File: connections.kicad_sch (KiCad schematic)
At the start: 0 parts

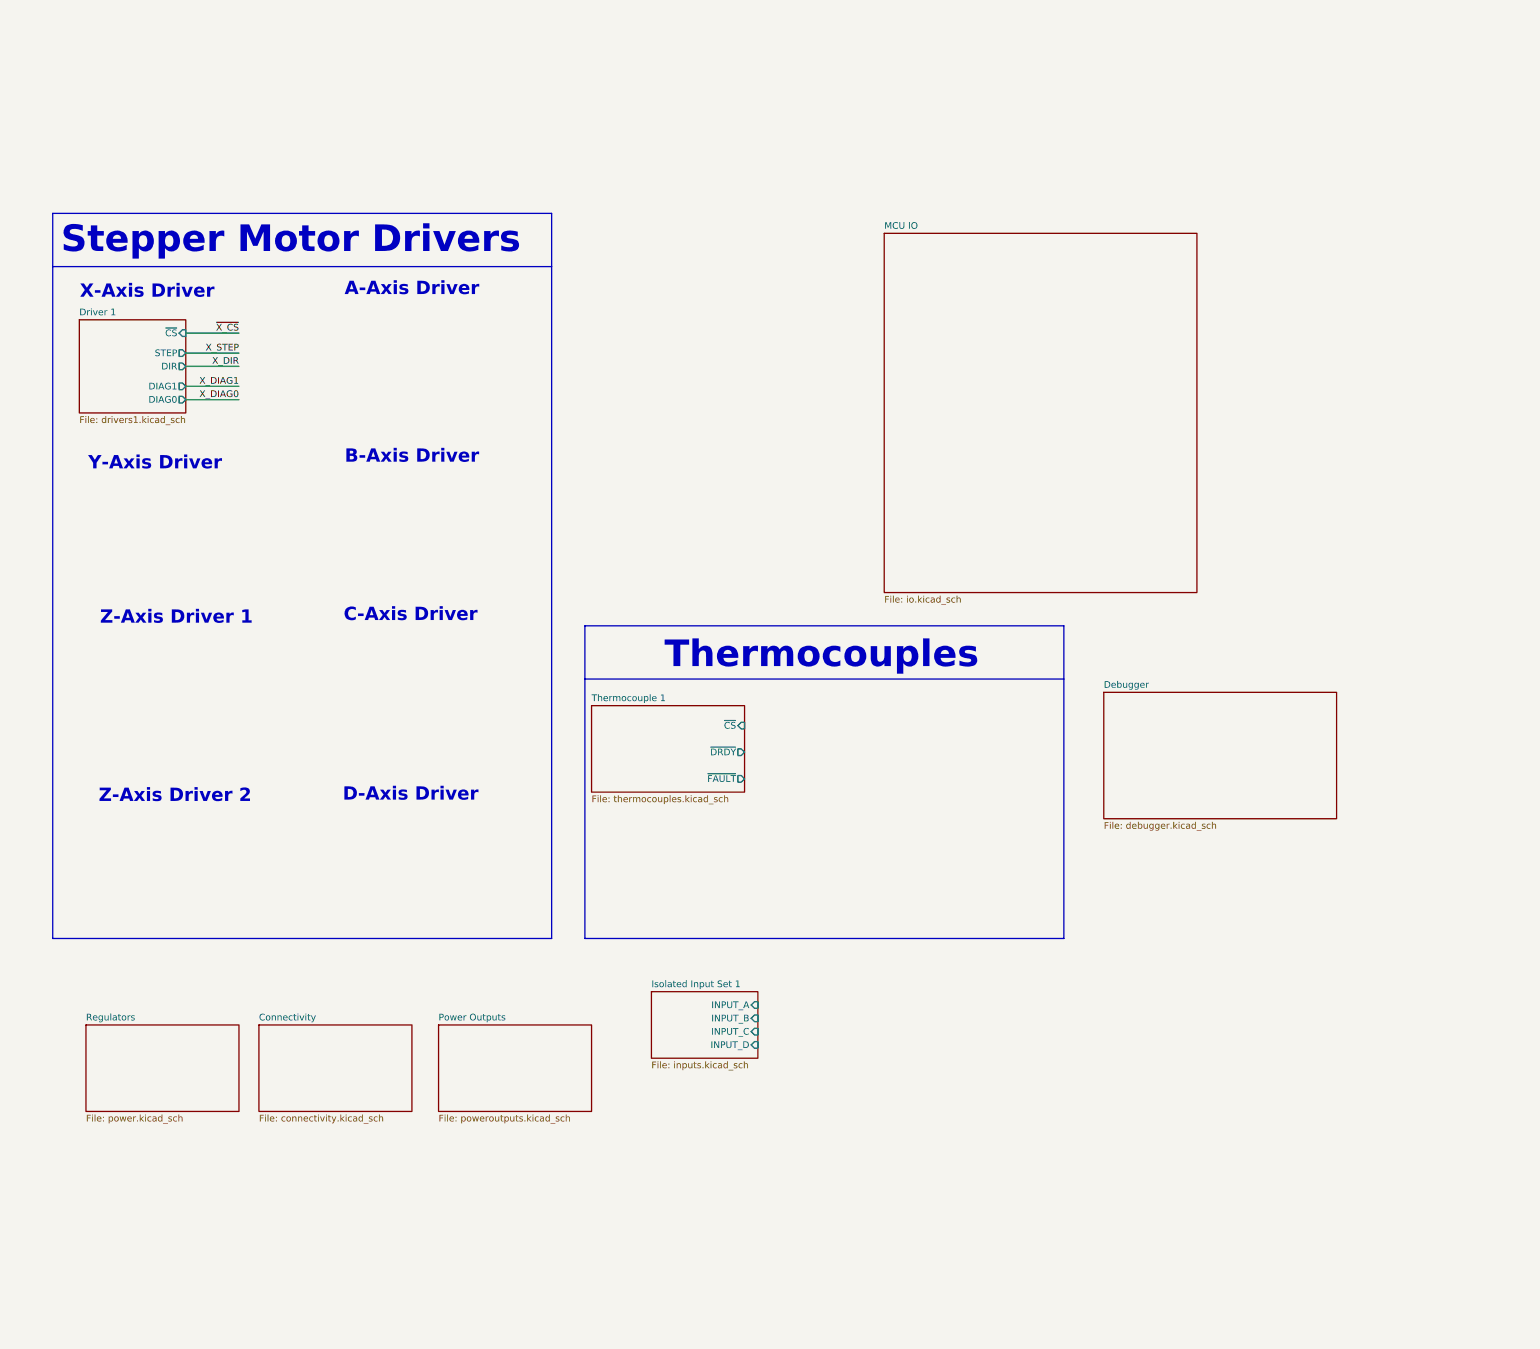
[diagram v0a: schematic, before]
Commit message: Soften scope, begin layout, reorganize sheets (still need to delete extras)
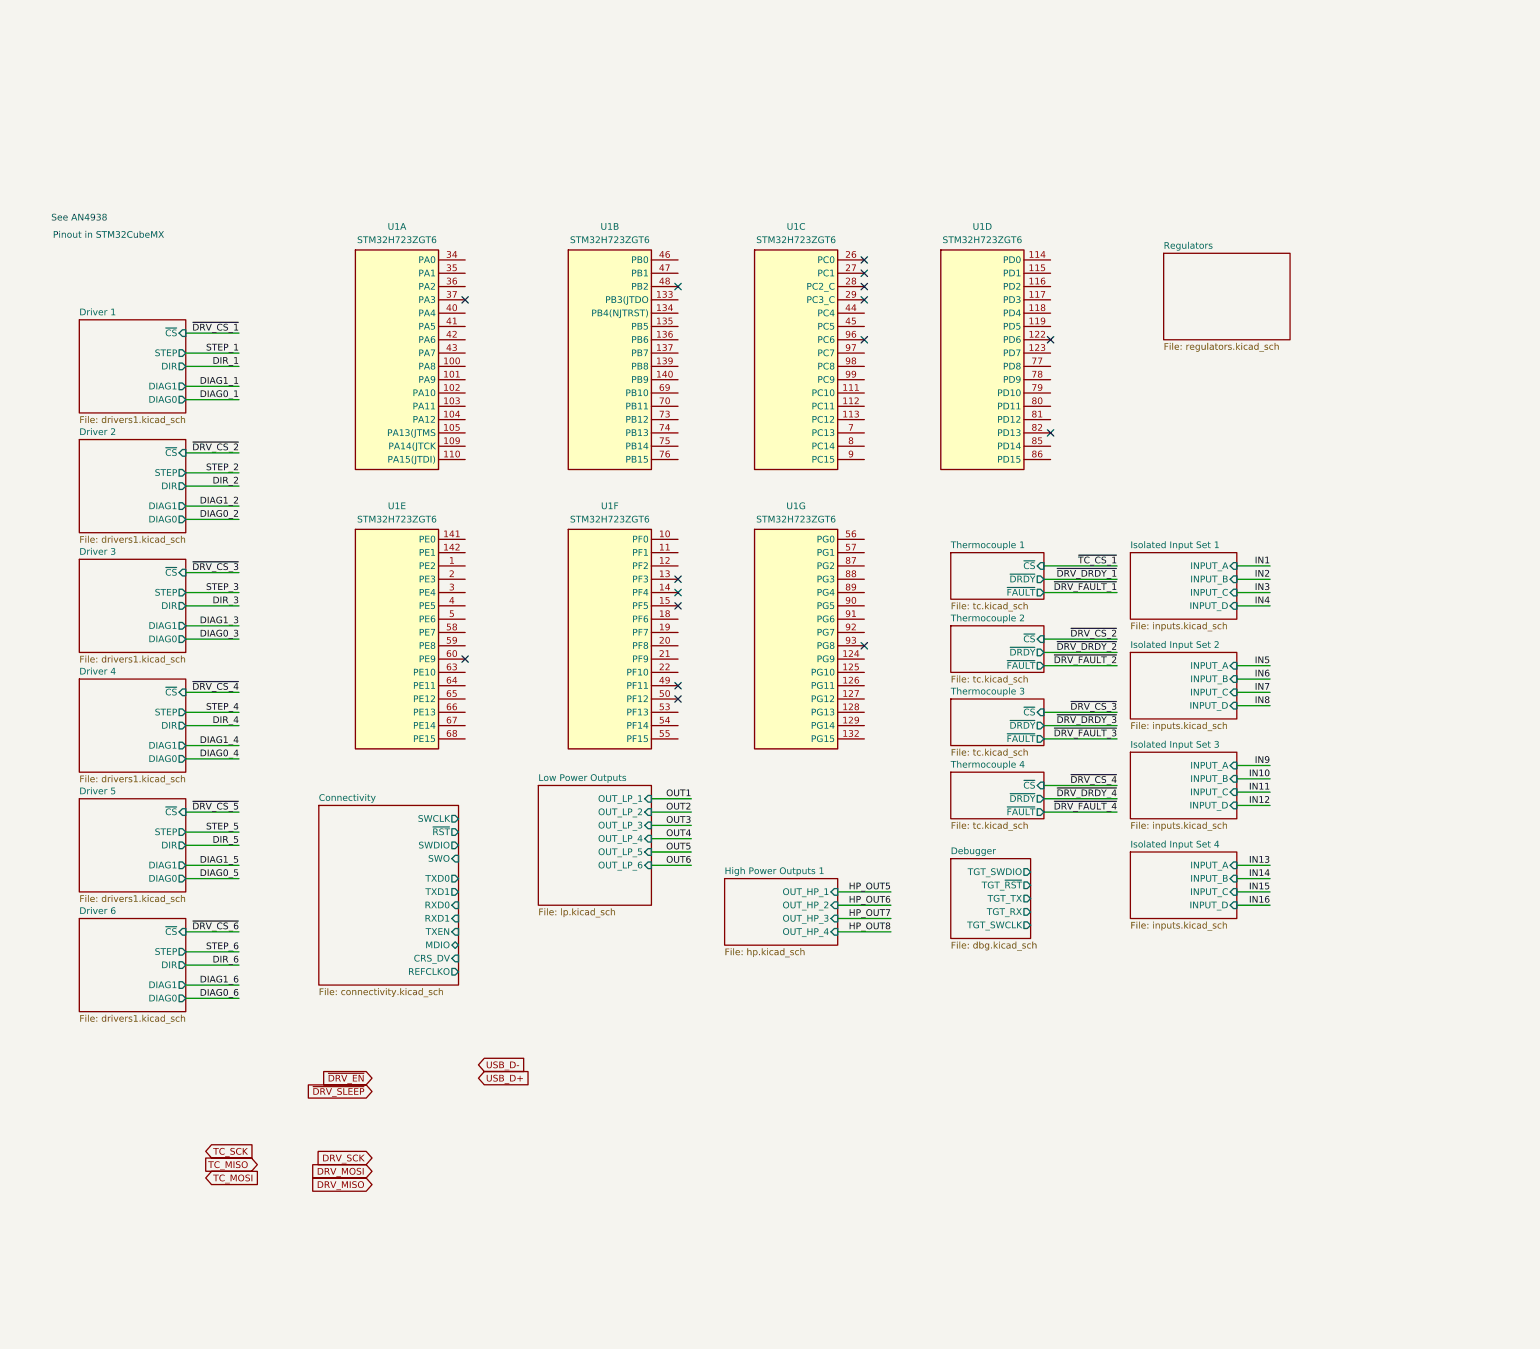
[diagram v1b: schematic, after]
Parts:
- added U1: STM32H723ZGT6, Package_QFP:LQFP-144_20x20mm_P0.5mm, symbol libserie:STM32H723ZGTx
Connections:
- no-connect marks 0 -> 16
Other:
- removed sheet MCU IO
- removed sheet Power Outputs
- added sheet Driver 2 (drivers1.kicad_sch)
- added sheet Driver 3 (drivers1.kicad_sch)
- added sheet Driver 4 (drivers1.kicad_sch)
- added sheet Driver 5 (drivers1.kicad_sch)
- added sheet Driver 6 (drivers1.kicad_sch)
- added sheet High Power Outputs 1 (hp.kicad_sch)
- added sheet Isolated Input Set 2 (inputs.kicad_sch)
- added sheet Isolated Input Set 3 (inputs.kicad_sch)
- added sheet Isolated Input Set 4 (inputs.kicad_sch)
- added sheet Low Power Outputs (lp.kicad_sch)
- added sheet Thermocouple 2 (tc.kicad_sch)
- added sheet Thermocouple 3 (tc.kicad_sch)
- added sheet Thermocouple 4 (tc.kicad_sch)
- sheet Connectivity ports: added CRS_DV, MDIO, REFCLKO, RXD0, RXD1, SWCLK, SWDIO, SWO, TXD0, TXD1, TXEN, ~{RST}; removed none
- sheet Debugger: file debugger.kicad_sch -> dbg.kicad_sch
- sheet Debugger ports: added TGT_RX, TGT_SWCLK, TGT_SWDIO, TGT_TX, TGT_~{RST}; removed none
- sheet Regulators: file power.kicad_sch -> regulators.kicad_sch
- sheet Thermocouple 1: file thermocouples.kicad_sch -> tc.kicad_sch
- note added: "Pinout in STM32CubeMX"
- note added: "See AN4938"
- note removed: "A-Axis Driver"
- note removed: "B-Axis Driver"
- note removed: "C-Axis Driver"
- note removed: "D-Axis Driver"
- note removed: "Stepper Motor Drivers"
- note removed: "Thermocouples"
- note removed: "X-Axis Driver"
- note removed: "Y-Axis Driver"
- note removed: "Z-Axis Driver 1"
- note removed: "Z-Axis Driver 2"

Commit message: ???
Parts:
- added J1: Conn_02x05_Odd_Even, Connector_PinHeader_2.54mm:PinHeader_1x10_P2.54mm_Vertical, symbol Connector_Generic:Conn_02x05_Odd_Even
- added J2, J3: Conn_02x20_Counter_Clockwise, symbol Connector_Generic:Conn_02x20_Counter_Clockwise
- added U2: STM32H723ZGT6, Package_QFP:LQFP-144_20x20mm_P0.5mm, symbol libserie:STM32H723ZGTx
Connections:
- new net +3.3V: J1.1 (Pin_1), U2.100 (PA8), U2.101 (PA9), U2.102 (PA10), U2.103 (PA11), U2.104 (PA12), U2.105 (PA13(JTMS), U2.34 (PA0), U2.35 (PA1), U2.36 (PA2), U2.37 (PA3), U2.40 (PA4), U2.41 (PA5), U2.42 (PA6), U2.43 (PA7)
- new net GND: J1.3 (Pin_3), J1.5 (Pin_5), J1.9 (Pin_9), U2.109 (PA14(JTCK), U2.110 (PA15(JTDI))
- new net SWCLK: J1.4 (Pin_4)
- new net SWDIO: J1.2 (Pin_2)
- new net SWO: J1.6 (Pin_6)
- new net ~{RST}: J1.10 (Pin_10)
- no-connect marks 16 -> 18
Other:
- sheet Connectivity renamed USB and Sensors
- removed sheet Isolated Input Set 3
- removed sheet Isolated Input Set 4
- removed sheet Thermocouple 3
- removed sheet Thermocouple 4
- added sheet High Power Outputs 2 (hp.kicad_sch)
- sheet USB and Sensors: file connectivity.kicad_sch -> misc.kicad_sch
- note added: "All these blocks need to be re-sync'd"
- note added: "I/O"
- note added: "Main Connections Sheet"
- note added: "Motor Drivers"

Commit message: loadcell math coming soon(tm)
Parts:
- removed J3: Conn_02x20_Counter_Clockwise, symbol Connector_Generic:Conn_02x20_Counter_Clockwise
- added C1: 100nF, APRLPrints:C_0603, symbol Device:C_Small
- added C2, C3: 2.2uF, APRLPrints:C_0603, symbol Device:C_Small
- added C4, C5: 10pF, APRLPrints:C_0603, symbol Device:C_Small
- added SW1: SKRPANE010, APRLPrints:SKRPANE010, symbol Switch:SW_MEC_5E
- added unit 8 of U1
- added Y1: 25 MHz, APRLPrints:3225-4P-L, symbol Device:Crystal_GND24_Small
- J1: footprint Connector_PinHeader_2.54mm:PinHeader_1x10_P2.54mm_Vertical -> Connector_PinHeader_1.00mm:PinHeader_2x05_P1.00mm_Vertical_SMD
- J2: footprint (none) -> Connector_PinHeader_1.00mm:PinHeader_2x20_P1.00mm_Vertical_SMD
- renumbered U2 to U1
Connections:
- net +3.3V: now also U1.108 (VDD), U1.121 (VDD), U1.131 (VDD), U1.144 (VDD), U1.17 (VDD), U1.30 (VDD), U1.33 (VDDA), U1.39 (VDD), U1.52 (VDD), U1.6 (VBAT), U1.62 (VDD), U1.72 (VDD), U1.84 (VDD), U1.95 (VDD33USB), C1.2, U1.143 (PDR_ON), U1.32 (VREF+); no longer U1.100 (PA8), U1.101 (PA9), U1.102 (PA10), U1.103 (PA11), U1.104 (PA12), U1.105 (PA13(JTMS), U1.34 (PA0), U1.35 (PA1), U1.36 (PA2), U1.37 (PA3), U1.40 (PA4), U1.41 (PA5), U1.42 (PA6), U1.43 (PA7)
- net DIAG0_1: now also U1.8 (PC14)
- net DIAG0_2: now also U1.2 (PE3)
- net DIAG0_3: now also U1.139 (PB8)
- net DIAG0_4: now also U1.132 (PG15)
- net DIAG0_5: now also U1.117 (PD3)
- net DIAG0_6: now also U1.112 (PC11)
- net DIAG1_1: now also U1.7 (PC13)
- net DIAG1_2: now also U1.1 (PE2)
- net DIAG1_3: now also U1.137 (PB7)
- net DIAG1_4: now also U1.129 (PG14)
- net DIAG1_5: now also U1.118 (PD4)
- net DIAG1_6: now also U1.113 (PC12)
- net DIR_1: now also U1.9 (PC15)
- net DIR_2: now also U1.3 (PE4)
- net DIR_3: now also U1.140 (PB9)
- net DIR_4: now also U1.134 (PB4(NJTRST))
- net DIR_5: now also U1.125 (PG10)
- net DIR_6: now also U1.114 (PD0)
- net DRV_MISO: now also U1.124 (PG9)
- net DRV_MOSI: now also U1.123 (PD7)
- net DRV_SCK: now also U1.126 (PG11)
- net GND: now also U1.107 (VSS), U1.120 (VSS), U1.130 (VSS), U1.16 (VSS), U1.31 (VSSA), U1.38 (VSS), U1.51 (VSS), U1.61 (VSS), U1.83 (VSS), U1.94 (VSS), C1.1, C2.1, C3.1, C4.1, C5.1, SW1.3 (K), SW1.4 (A), U1.138 (BOOT0), Y1.2 (G), Y1.4 (G); no longer U1.109 (PA14(JTCK), U1.110 (PA15(JTDI))
- net STEP_1: now also U1.10 (PF0)
- net STEP_2: now also U1.4 (PE5)
- net STEP_3: now also U1.141 (PE0)
- net STEP_4: now also U1.135 (PB5)
- net STEP_5: now also U1.127 (PG12)
- net STEP_6: now also U1.115 (PD1)
- net SWCLK: now also U1.109 (PA14(JTCK)
- net SWDIO: now also U1.105 (PA13(JTMS)
- net SWO: now also U1.133 (PB3(JTDO)
- net ~{DRV_CS_1}: now also U1.11 (PF1)
- net ~{DRV_CS_2}: now also U1.5 (PE6)
- net ~{DRV_CS_3}: now also U1.142 (PE1)
- net ~{DRV_CS_4}: now also U1.136 (PB6)
- net ~{DRV_CS_5}: now also U1.128 (PG13)
- net ~{DRV_CS_6}: now also U1.116 (PD2)
- net ~{RST}: now also SW1.1, SW1.2, U1.25 (NRST)
- net MCU_USB_D-: now reaches U1.103 (PA11)
- net MCU_USB_D+: now reaches U1.104 (PA12)
- new net: C5.2, U1.23 (PH0), Y1.3
- new net: C4.2, U1.24 (PH1), Y1.1
- new net: C3.2, U1.106 (VCAP)
- new net: C2.2, U1.71 (VCAP)
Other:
- sheet Debugger renamed Debugger and USB
- sheet USB and Sensors renamed Sensors
- sheet Debugger and USB ports: added TGT_RST, TGT_SWO; removed TGT_RX, TGT_TX, TGT_~{RST}
- sheet High Power Outputs 1 ports: added OUT_HP_A, OUT_HP_B; removed OUT_HP_1, OUT_HP_2, OUT_HP_3, OUT_HP_4
- sheet High Power Outputs 2 ports: added OUT_HP_A, OUT_HP_B; removed OUT_HP_1, OUT_HP_2, OUT_HP_3, OUT_HP_4
- sheet Low Power Outputs ports: added none; removed OUT_LP_4, OUT_LP_5, OUT_LP_6
- sheet Sensors: file misc.kicad_sch -> sense.kicad_sch
- sheet Sensors ports: added A0, A1, A2, DIN, DOUT, LC_INT, PIEZO, SCL, SCLK, SDA, TOGGLE, TS_ALRT/RDY, ~{LC_CS}, ~{LC_DRDY}; removed CRS_DV, MDIO, REFCLKO, RXD0, RXD1, SWCLK, SWDIO, SWO, TXD0, TXD1, TXEN, ~{RST}
- sheet Thermocouple 1 ports: added none; removed ~{FAULT}
- sheet Thermocouple 2 ports: added none; removed ~{FAULT}
- note removed: "All these blocks need to be re-sync'd"
- moved on the sheet: J2

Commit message: a
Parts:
- removed C1: 100nF, APRLPrints:C_0603, symbol Device:C_Small
- removed J1: Conn_02x05_Odd_Even, Connector_PinHeader_1.00mm:PinHeader_2x05_P1.00mm_Vertical_SMD, symbol Connector_Generic:Conn_02x05_Odd_Even
- added J2: Conn_02x20_Counter_Clockwise, Connector_IDC:IDC-Header_2x20_P2.54mm_Vertical_SMD, symbol Connector_Generic:Conn_02x20_Odd_Even
- added J3: Conn_ARM_SWD_TagConnect_TC2030-NL, Connector:Tag-Connect_TC2030-IDC-NL_2x03_P1.27mm_Vertical, symbol Connector:Conn_ARM_SWD_TagConnect_TC2030-NL
- J1: renamed from J2; footprint Connector_PinHeader_1.00mm:PinHeader_2x20_P1.00mm_Vertical_SMD -> Connector_IDC:IDC-Header_2x20_P2.54mm_Vertical_SMD; symbol Connector_Generic:Conn_02x20_Counter_Clockwise -> Connector_Generic:Conn_02x20_Odd_Even
- renumbered C4 to C1, C5 to C2, C2 to C3, C3 to C4
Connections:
- net +3.3V: now also J3.1 (VCC)
- net DIAG0_1: no longer U1.8 (PC14)
- net DIAG0_2: no longer U1.2 (PE3)
- net DIAG0_3: no longer U1.139 (PB8)
- net DIAG0_4: no longer U1.132 (PG15)
- net DIAG0_5: no longer U1.117 (PD3)
- net DIAG0_6: no longer U1.112 (PC11)
- net DIR_1: no longer U1.9 (PC15)
- net DIR_2: no longer U1.3 (PE4)
- net DIR_3: no longer U1.140 (PB9)
- net DIR_4: no longer U1.134 (PB4(NJTRST))
- net DIR_5: no longer U1.125 (PG10)
- net DIR_6: no longer U1.114 (PD0)
- net GND: now also J1.1 (Pin_1), J1.11 (Pin_11), J1.13 (Pin_13), J1.15 (Pin_15), J1.17 (Pin_17), J1.19 (Pin_19), J1.21 (Pin_21), J1.23 (Pin_23), J1.25 (Pin_25), J1.27 (Pin_27), J1.29 (Pin_29), J1.3 (Pin_3), J1.31 (Pin_31), J1.33 (Pin_33), J1.35 (Pin_35), J1.37 (Pin_37), J1.39 (Pin_39), J1.5 (Pin_5), J1.7 (Pin_7), J1.9 (Pin_9), J2.1 (Pin_1), J2.11 (Pin_11), J2.13 (Pin_13), J2.15 (Pin_15), J2.17 (Pin_17), J2.19 (Pin_19), J2.21 (Pin_21), J2.23 (Pin_23), J2.25 (Pin_25), J2.27 (Pin_27), J2.29 (Pin_29), J2.3 (Pin_3), J2.31 (Pin_31), J2.33 (Pin_33), J2.35 (Pin_35), J2.37 (Pin_37), J2.39 (Pin_39), J2.5 (Pin_5), J2.7 (Pin_7), J2.9 (Pin_9), J3.5 (GND)
- net STEP_1: no longer U1.10 (PF0)
- net STEP_2: no longer U1.4 (PE5)
- net STEP_3: no longer U1.141 (PE0)
- net STEP_4: no longer U1.135 (PB5)
- net STEP_5: no longer U1.127 (PG12)
- net STEP_6: no longer U1.115 (PD1)
- net SWCLK: now also J3.4 (SWCLK)
- net SWDIO: now also J3.2 (SWDIO)
- net ~{DRV_CS_1}: no longer U1.11 (PF1)
- net ~{DRV_CS_2}: no longer U1.5 (PE6)
- net ~{DRV_CS_3}: no longer U1.142 (PE1)
- net ~{DRV_CS_4}: no longer U1.136 (PB6)
- net ~{DRV_CS_5}: no longer U1.128 (PG13)
- net ~{DRV_CS_6}: no longer U1.116 (PD2)
- net ~{RST}: now also J3.3 (~{RESET})
- net DIAG1_1: no longer names the net of U1.7 (PC13)
- net DIAG1_2: no longer names the net of U1.1 (PE2)
- net DIAG1_3: no longer names the net of U1.137 (PB7)
- net DIAG1_4: no longer names the net of U1.129 (PG14)
- net DIAG1_5: no longer names the net of U1.118 (PD4)
- net DIAG1_6: no longer names the net of U1.113 (PC12)
- net DRV_MISO: no longer names the net of U1.124 (PG9)
- net DRV_MOSI: no longer names the net of U1.123 (PD7)
- net DRV_SCK: no longer names the net of U1.126 (PG11)
- net SWO: no longer names the net of U1.133 (PB3(JTDO)
- no-connect marks 18 -> 17
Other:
- sheet Sensors renamed Sensors 1
- added sheet Driver 10 (drivers1.kicad_sch)
- added sheet Driver 7 (drivers1.kicad_sch)
- added sheet Driver 8 (drivers1.kicad_sch)
- added sheet Driver 9 (drivers1.kicad_sch)
- added sheet Sensors 2 (sense.kicad_sch)
- added sheet Thermistors (ths.kicad_sch)
- sheet Debugger and USB ports: added none; removed TGT_SWO
- sheet Driver 1 ports: added none; removed DIAG1
- sheet Driver 2 ports: added none; removed DIAG1
- sheet Driver 3 ports: added none; removed DIAG1
- sheet Driver 4 ports: added none; removed DIAG1
- sheet Driver 5 ports: added none; removed DIAG1
- sheet Driver 6 ports: added none; removed DIAG1
- sheet Low Power Outputs ports: added OUT_LP_4, OUT_LP_5, OUT_LP_6, TACH1, TACH2, TACH3, TACH4, TACH5, TACH6; removed none
- sheet Sensors 1 ports: added none; removed TS_ALRT/RDY
- sheet Thermocouple 1 ports: added none; removed ~{DRDY}
- sheet Thermocouple 2 ports: added none; removed ~{DRDY}
- note added: "On the top: 1. CS SCK MOSI MISO 2. STEP 3. DIR 4. DIAG0 Go reverse direction for bottom steppers SPI1 for all motors Do not mix SPI lines with other things SPI2 for thermocouples SPI4/5/6 are broken out for external additions SPI3 unused"
- moved on the sheet: C1, C2, J1, Y1
